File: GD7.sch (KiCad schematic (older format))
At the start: 19 parts, among them IC3 HCPL-316J, IC4 IXDD614PI, P10 CONN_01X03, P11 CONN_01X03

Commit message: uding HCPL-361J modified symbol
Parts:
- IC3: symbol HCPL-316J-RESCUE-gatedrive -> HCPL-316J
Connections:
- wire segments 41 -> 50
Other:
- moved on the sheet: IC4
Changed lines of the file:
@@
 EESchema Schematic File Version 2
-LIBS:gatedrive-rescue
 LIBS:power
 LIBS:device
@@
 LIBS:contrib
 LIBS:valves
-LIBS:GateDrive
+LIBS:74xgxx
+LIBS:ac-dc
+LIBS:actel
+LIBS:Altera
+LIBS:analog_devices
+LIBS:brooktre
+LIBS:cmos_ieee
+LIBS:dc-dc
+LIBS:diode
+LIBS:elec-unifil
+LIBS:ESD_Protection
+LIBS:ftdi
+LIBS:gennum
+LIBS:graphic
+LIBS:hc11
+LIBS:ir
+LIBS:Lattice
+LIBS:logo
+LIBS:maxim
+LIBS:microchip_dspic33dsc
+LIBS:microchip_pic10mcu
+LIBS:microchip_pic12mcu
+LIBS:microchip_pic16mcu
+LIBS:microchip_pic18mcu
+LIBS:microchip_pic32mcu
+LIBS:motor_drivers
+LIBS:msp430
+LIBS:nordicsemi
+LIBS:nxp_armmcu
+LIBS:onsemi
+LIBS:Oscillators
+LIBS:powerint
+LIBS:Power_Management
+LIBS:pspice
+LIBS:references
+LIBS:relays
+LIBS:rfcom
+LIBS:sensors
+LIBS:silabs
+LIBS:stm8
+LIBS:stm32
+LIBS:supertex
+LIBS:switches
+LIBS:transf
+LIBS:ttl_ieee
+LIBS:video
+LIBS:Worldsemi
+LIBS:Xicor
+LIBS:Zilog
 LIBS:gatedrive-cache
 EELAYER 25 0
@@
 L IXDD614PI-RESCUE-gatedrive IC4
 U 1 1 56EFA9D0
-P 7900 5100
-F 0 "IC4" H 7900 4900 60  0000 C CNN
-F 1 "IXDD614PI" H 7950 5450 60  0000 C CNN
-F 2 "gatedrive:DIP-8_W7.62mm_LongPads" H 7900 5200 60  0001 C CNN
-F 3 "" H 7900 5200 60  0000 C CNN
-F 4 "CHINA[already bought]" H 7900 5100 60  0001 C CNN "Supplier"
-	1    7900 5100
-	1    0    0    -1
-$EndComp
-$Comp
-L HCPL-316J-RESCUE-gatedrive IC3
+P 7950 5100
+AR Path="/56EFA9D0" Ref="IC4"  Part="1"
+AR Path="/56EF0567/56EFA9D0" Ref="IC4"  Part="1"
+F 0 "IC4" H 7950 4900 60  0000 C CNN
+F 1 "IXDD614PI" H 8000 5450 60  0000 C CNN
+F 2 "gatedrive:DIP-8_W7.62mm_LongPads" H 7950 5200 60  0001 C CNN
+F 3 "" H 7950 5200 60  0000 C CNN
+F 4 "CHINA[already bought]" H 7950 5100 60  0001 C CNN "Supplier"
+	1    7950 5100
+	1    0    0    -1
+$EndComp
+$Comp
+L HCPL-316J IC3
 U 1 1 56EFA9D1
-P 5550 4750
-F 0 "IC3" H 5550 4150 60  0000 C CNN
-F 1 "HCPL-316J" H 5300 5200 60  0000 C CNN
-F 2 "Housings_SOIC:SOIC-16_7.5x10.3mm_Pitch1.27mm" H 5550 4750 60  0001 C CNN
-F 3 "" H 5550 4750 60  0000 C CNN
-F 4 "CHINA [ already bought]" H 5550 4750 60  0001 C CNN "Supplier"
-	1    5550 4750
+P 5650 4850
+F 0 "IC3" H 5350 4400 60  0000 C CNN
+F 1 "HCPL-316J" H 5400 5350 60  0000 C CNN
+F 2 "Housings_SOIC:SOIC-16_7.5x10.3mm_Pitch1.27mm" H 5650 4850 60  0001 C CNN
+F 3 "" H 5650 4850 60  0000 C CNN
+F 4 "CHINA [ already bought]" H 5650 4850 60  0001 C CNN "Supplier"
+	1    5650 4850
 	1    0    0    -1
 $EndComp
@@
 Text GLabel 6450 4800 2    60   Input ~ 0
 15V7
-Text GLabel 7500 4850 0    60   Input ~ 0
-15V7
-Text GLabel 7500 5150 0    60   Input ~ 0
--5V7
-Text GLabel 8350 5150 2    60   Input ~ 0
+Text GLabel 7550 4850 0    60   Input ~ 0
+15V7
+Text GLabel 7550 5150 0    60   Input ~ 0
+-5V7
+Text GLabel 8300 5150 2    60   Input ~ 0
 -5V7
 Text GLabel 10200 4950 2    60   Input ~ 0
@@
 a cap to ensure soft turn-off, recommended by datasheet of hcpl.
 Wire Wire Line
-	6950 4950 7500 4950
-Wire Wire Line
-	6250 4950 6650 4950
-Wire Wire Line
-	6250 5050 6250 5150
-Wire Wire Line
-	6250 4750 6250 4850
+	6950 4950 7150 4950
+Wire Wire Line
+	7150 4950 7550 4950
+Wire Wire Line
+	5850 4950 6500 4950
+Wire Wire Line
+	6500 4950 6650 4950
+Wire Wire Line
+	5850 5050 6250 5100
+Wire Wire Line
+	6250 5100 5850 5150
+Wire Wire Line
+	5850 4750 6250 4800
+Wire Wire Line
+	6250 4800 5850 4850
 Connection ~ 6550 4100
 Wire Wire Line
-	6550 4650 6250 4650
+	6550 4650 5850 4650
 Wire Wire Line
 	6550 4100 6650 4100
 Wire Wire Line
-	6550 4050 6550 4650
+	6550 4050 6550 4100
+Wire Wire Line
+	6550 4100 6550 4650
 Connection ~ 8450 4950
 Wire Wire Line
@@
 Connection ~ 7150 4950
 Wire Wire Line
-	3625 4650 4850 4650
-Wire Wire Line
-	8350 4950 9050 4950
+	3625 4650 4000 4650
+Wire Wire Line
+	4000 4650 4950 4650
+Wire Wire Line
+	8300 4950 8450 4950
+Wire Wire Line
+	8450 4950 8900 4950
+Wire Wire Line
+	8900 4950 9050 4950
 Wire Wire Line
 	9350 4950 9450 4950
 Wire Wire Line
-	9750 4950 10200 4950
+	9750 4950 9950 4950
+Wire Wire Line
+	9950 4950 10200 4950
 Wire Wire Line
 	9750 5250 9950 5250
@@
 Connection ~ 9950 4950
 Wire Wire Line
-	8350 5050 8450 5050
+	8300 5050 8450 5050
 Wire Wire Line
 	8450 5050 8450 4950
@@
 	4400 4350 4400 4550
 Wire Wire Line
-	4400 4550 4850 4550
+	4400 4550 4950 4550
 Wire Wire Line
 	4000 4350 4000 4650
@@
 	4000 5300 4000 4750
 Wire Wire Line
-	4000 4750 4850 4750
-Wire Wire Line
-	4850 5150 4750 5150
+	4000 4750 4950 4750
+Wire Wire Line
+	4950 5150 4750 5150
 Wire Wire Line
 	4750 5150 4750 5300
 Wire Wire Line
-	4850 4850 4400 4850
+	4950 4850 4400 4850
 Wire Wire Line
 	4400 4850 4400 5300
 Wire Wire Line
-	6250 4450 6300 4450
+	5850 4450 6300 4450
 Wire Wire Line
 	6300 4450 6300 4350
@@
 Wire Wire Line
 	6500 5000 6500 4950
-Text GLabel 8350 4850 2    60   Input ~ 0
+Text GLabel 8300 4850 2    60   Input ~ 0
 15V7
 Text GLabel 7125 5100 3    60   Input ~ 0
 15V7
 Wire Wire Line
-	7125 5050 7500 5050
+	7125 5050 7550 5050
 Text HLabel 900  3800 3    60   Input ~ 0
 T7
-Text HLabel 4850 4450 0    60   Input ~ 0
+Text HLabel 4950 4450 0    60   Input ~ 0
 T7
 Text GLabel 4450 2300 3    60   Input ~ 0
@@
 Text GLabel 4400 4350 1    60   Input ~ 0
 GND1
-Text GLabel 4850 4950 0    60   Input ~ 0
+Text GLabel 4950 4950 0    60   Input ~ 0
 ~FAULT
 Text GLabel 4750 5300 3    60   Input ~ 0

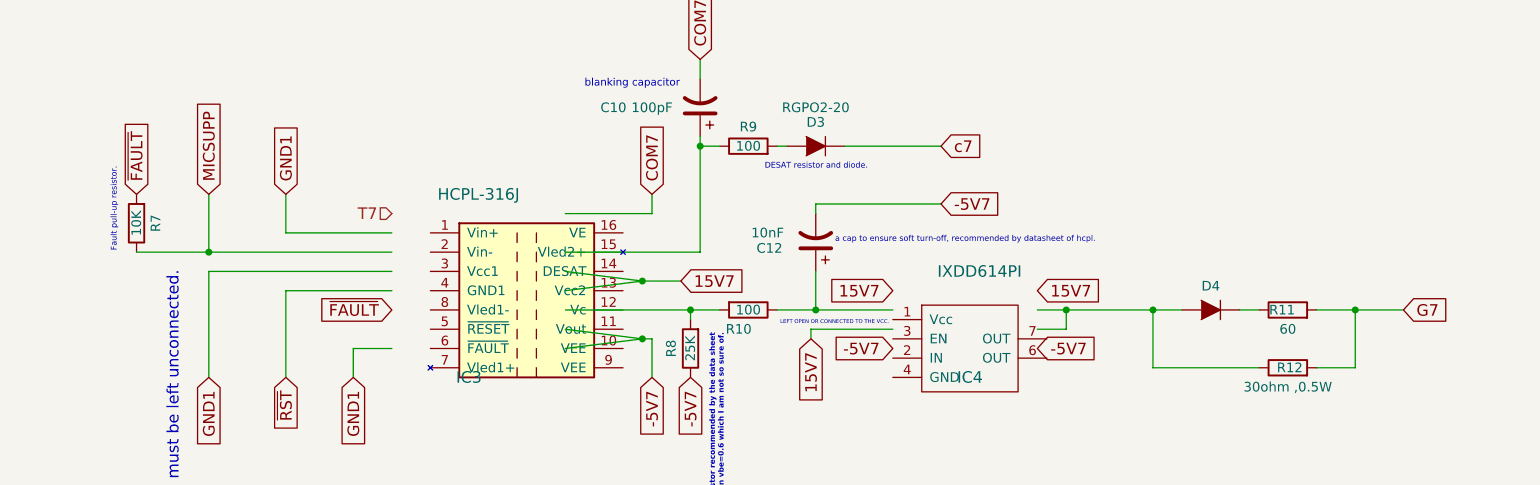
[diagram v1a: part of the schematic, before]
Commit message: cleaning the schematic
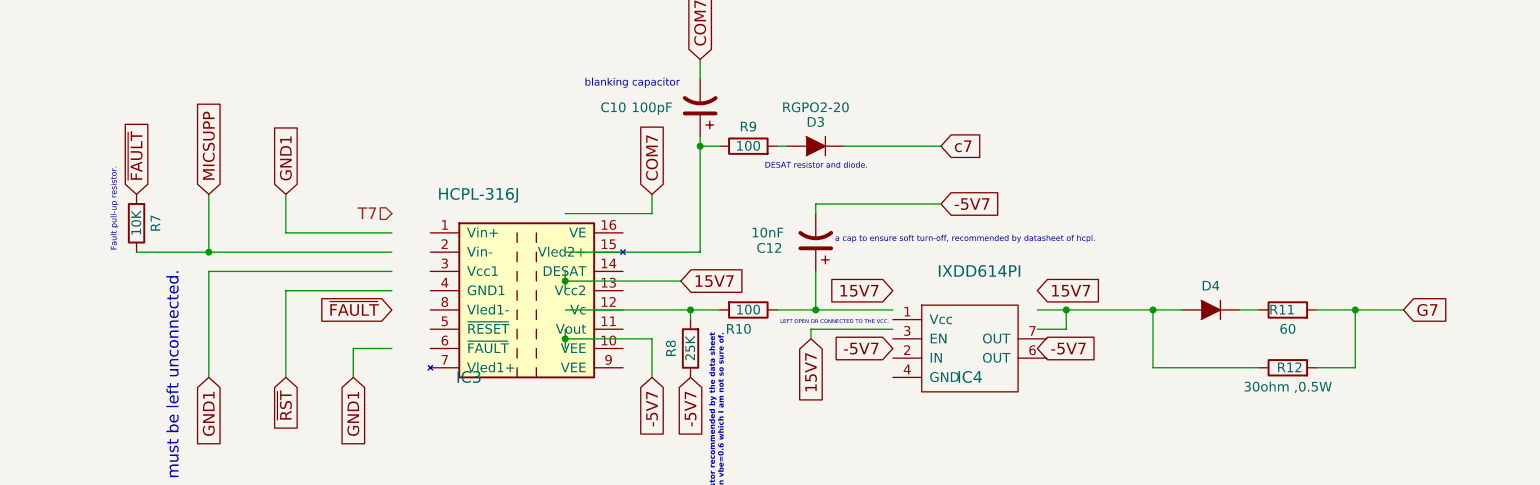
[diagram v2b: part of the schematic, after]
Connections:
- wire segments 50 -> 41
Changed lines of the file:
@@
 a cap to ensure soft turn-off, recommended by datasheet of hcpl.
 Wire Wire Line
-	6950 4950 7150 4950
+	6950 4950 7550 4950
 Wire Wire Line
-	7150 4950 7550 4950
+	5850 4950 6650 4950
 Wire Wire Line
-	5850 4950 6500 4950
+	5850 5050 5850 5150
 Wire Wire Line
-	6500 4950 6650 4950
-Wire Wire Line
-	5850 5050 6250 5100
-Wire Wire Line
-	6250 5100 5850 5150
-Wire Wire Line
-	5850 4750 6250 4800
-Wire Wire Line
-	6250 4800 5850 4850
+	5850 4750 5850 4850
 Connection ~ 6550 4100
 Wire Wire Line
@@
 	6550 4100 6650 4100
 Wire Wire Line
-	6550 4050 6550 4100
-Wire Wire Line
-	6550 4100 6550 4650
+	6550 4050 6550 4650
 Connection ~ 8450 4950
 Wire Wire Line
@@
 Connection ~ 7150 4950
 Wire Wire Line
-	3625 4650 4000 4650
+	3625 4650 4950 4650
 Wire Wire Line
-	4000 4650 4950 4650
-Wire Wire Line
-	8300 4950 8450 4950
-Wire Wire Line
-	8450 4950 8900 4950
-Wire Wire Line
-	8900 4950 9050 4950
+	8300 4950 9050 4950
 Wire Wire Line
 	9350 4950 9450 4950
 Wire Wire Line
-	9750 4950 9950 4950
-Wire Wire Line
-	9950 4950 10200 4950
+	9750 4950 10200 4950
 Wire Wire Line
 	9750 5250 9950 5250
@@
 	6300 5300 6300 5100
 Wire Wire Line
-	6300 5100 6250 5100
-Connection ~ 6250 5100
+	6300 5100 5850 5100
+Connection ~ 5850 5100
 Wire Wire Line
-	6250 4800 6450 4800
-Connection ~ 6250 4800
+	5850 4800 6450 4800
+Connection ~ 5850 4800
 Wire Wire Line
 	8900 5250 9450 5250

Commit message: completion of the layout, initial layout of the protection circuit, reducing number of circuit to 7
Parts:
- C10, C11, C12, C13, C14, C8, C9: footprint Capacitors_ThroughHole:C_Disc_D3_P2.5 -> gatedrive:C_Disc
- D3: footprint Diodes_ThroughHole:Diode_DO-201AD_Horizontal_RM15 -> Diodes_ThroughHole:Diode_DO-41_SOD81_Horizontal_RM10
- R11, R12: footprint Resistors_ThroughHole:Resistor_Horizontal_RM20mm -> gatedrive:Resistor_multi
- R7: footprint Resistors_ThroughHole:Resistor_Vertical_RM5mm -> Resistors_ThroughHole:Resistor_Horizontal_RM10mm
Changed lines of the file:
@@
 EESchema Schematic File Version 2
+LIBS:Symbols_DCDC-ACDC-Converter_RevC_20Jul2012
+LIBS:Symbols_EN60617_13Mar2013
+LIBS:Symbols_EN60617-10_HF-Radio_DRAFT_12Sep2013
+LIBS:Symbols_ICs-Diskrete_RevD10
+LIBS:Symbols_ICs-Opto_RevB_16Sep2013
+LIBS:Symbols_Microcontroller_Philips-NXP_RevA_06Oct2013
+LIBS:SymbolsSimilarEN60617+oldDIN617-RevE8
+LIBS:Symbols_Socket-DIN41612_RevA
+LIBS:Symbols_Transformer-Diskrete_RevA
 LIBS:power
 LIBS:device
@@
 $Descr A4 11693 8268
 encoding utf-8
-Sheet 3 10
+Sheet 3 9
 Title "IGBT GATE DRIVE SCHEMATIC."
 Date "2016-03-02"
@@
 F 0 "D3" H 7150 3976 50  0000 C CNN
 F 1 "RGPO2-20" H 7150 3900 50  0000 C CNN
-F 2 "Diodes_ThroughHole:Diode_DO-201AD_Horizontal_RM15" H 7150 4100 50  0001 C CNN
+F 2 "Diodes_ThroughHole:Diode_DO-41_SOD81_Horizontal_RM10" H 7150 4100 50  0001 C CNN
 F 3 "" H 7150 4100 50  0000 C CNN
 F 4 "El-Amir" H 7150 4100 60  0001 C CNN "Supplier"
@@
 F 0 "R7" V 3525 4500 50  0000 C CNN
 F 1 "10K" V 3625 4500 50  0000 C CNN
-F 2 "Resistors_ThroughHole:Resistor_Vertical_RM5mm" V 3555 4500 50  0001 C CNN
+F 2 "Resistors_ThroughHole:Resistor_Horizontal_RM10mm" V 3555 4500 50  0001 C CNN
 F 3 "" H 3625 4500 50  0000 C CNN
 F 4 "EL AMIR" H 3625 4500 60  0001 C CNN "Supplier"
@@
 F 0 "C8" H 4150 2150 50  0000 C CNN
 F 1 "0.1uF" H 4250 2050 50  0000 C CNN
-F 2 "Capacitors_ThroughHole:C_Disc_D3_P2.5" H 4488 2000 50  0001 C CNN
+F 2 "gatedrive:C_Disc" H 4488 2000 50  0001 C CNN
 F 3 "" H 4450 2150 50  0000 C CNN
 F 4 "EL AMIR" H 4450 2150 60  0001 C CNN "Supplier"
@@
 F 0 "C10" H 7000 3900 50  0000 C CNN
 F 1 "100pF" H 6800 3900 50  0000 C CNN
-F 2 "Capacitors_ThroughHole:C_Disc_D3_P2.5" H 6588 3750 50  0001 C CNN
+F 2 "gatedrive:C_Disc" H 6588 3750 50  0001 C CNN
 F 3 "" H 6550 3900 50  0000 C CNN
 	1    6550 3900
@@
 F 0 "C14" H 8450 2150 50  0000 C CNN
 F 1 "0.1uF" H 8450 2050 50  0000 C CNN
-F 2 "Capacitors_ThroughHole:C_Disc_D3_P2.5" H 8888 2000 50  0001 C CNN
+F 2 "gatedrive:C_Disc" H 8888 2000 50  0001 C CNN
 F 3 "" H 8850 2150 50  0000 C CNN
 	1    8850 2150
@@
 F 0 "C13" H 7400 2150 50  0000 C CNN
 F 1 "0.1uF" H 7400 2050 50  0000 C CNN
-F 2 "Capacitors_ThroughHole:C_Disc_D3_P2.5" H 7788 2000 50  0001 C CNN
+F 2 "gatedrive:C_Disc" H 7788 2000 50  0001 C CNN
 F 3 "" H 7750 2150 50  0000 C CNN
 	1    7750 2150
@@
 F 0 "C9" H 5150 2150 50  0000 C CNN
 F 1 "0.1uF" H 5150 2050 50  0000 C CNN
-F 2 "Capacitors_ThroughHole:C_Disc_D3_P2.5" H 5538 2000 50  0001 C CNN
+F 2 "gatedrive:C_Disc" H 5538 2000 50  0001 C CNN
 F 3 "" H 5500 2150 50  0000 C CNN
 	1    5500 2150
@@
 F 0 "C11" H 6300 2150 50  0000 R CNN
 F 1 "330pF" H 6400 2050 50  0000 R CNN
-F 2 "Capacitors_ThroughHole:C_Disc_D3_P2.5" H 6638 2000 50  0001 C CNN
+F 2 "gatedrive:C_Disc" H 6638 2000 50  0001 C CNN
 F 3 "" H 6600 2150 50  0000 C CNN
 	1    6600 2150
@@
 LEFT OPEN OR CONNECTED TO THE VCC.
 $Comp
-L PWR_FLAG #FLG08
+L PWR_FLAG #FLG01
 U 1 1 56EFA9DE
 P 1300 3800
-F 0 "#FLG08" H 1300 3895 50  0001 C CNN
+F 0 "#FLG01" H 1300 3895 50  0001 C CNN
 F 1 "PWR_FLAG" H 1300 4024 50  0000 C CNN
 F 2 "" H 1300 3800 50  0000 C CNN
@@
 $EndComp
 $Comp
-L PWR_FLAG #FLG09
+L PWR_FLAG #FLG02
 U 1 1 56EFA9DF
 P 1750 3800
-F 0 "#FLG09" H 1750 3895 50  0001 C CNN
+F 0 "#FLG02" H 1750 3895 50  0001 C CNN
 F 1 "PWR_FLAG" H 1750 4024 50  0000 C CNN
 F 2 "" H 1750 3800 50  0000 C CNN
@@
 $EndComp
 $Comp
-L PWR_FLAG #FLG010
+L PWR_FLAG #FLG03
 U 1 1 56EFA9E0
 P 1750 2650
-F 0 "#FLG010" H 1750 2745 50  0001 C CNN
+F 0 "#FLG03" H 1750 2745 50  0001 C CNN
 F 1 "PWR_FLAG" H 1750 2874 50  0000 C CNN
 F 2 "" H 1750 2650 50  0000 C CNN
@@
 $EndComp
 $Comp
-L PWR_FLAG #FLG011
+L PWR_FLAG #FLG04
 U 1 1 56EFA9E1
 P 900 2650
-F 0 "#FLG011" H 900 2745 50  0001 C CNN
+F 0 "#FLG04" H 900 2745 50  0001 C CNN
 F 1 "PWR_FLAG" H 900 2874 50  0000 C CNN
 F 2 "" H 900 2650 50  0000 C CNN
@@
 $EndComp
 $Comp
-L PWR_FLAG #FLG012
+L PWR_FLAG #FLG05
 U 1 1 56EFA9E2
 P 1300 2650
-F 0 "#FLG012" H 1300 2745 50  0001 C CNN
+F 0 "#FLG05" H 1300 2745 50  0001 C CNN
 F 1 "PWR_FLAG" H 1300 2874 50  0000 C CNN
 F 2 "" H 1300 2650 50  0000 C CNN
@@
 $EndComp
 $Comp
-L PWR_FLAG #FLG013
+L PWR_FLAG #FLG06
 U 1 1 56EFA9E3
 P 900 3800
-F 0 "#FLG013" H 900 3895 50  0001 C CNN
+F 0 "#FLG06" H 900 3895 50  0001 C CNN
 F 1 "PWR_FLAG" H 900 4024 50  0000 C CNN
 F 2 "" H 900 3800 50  0000 C CNN
@@
 F 0 "C12" H 7390 4630 50  0000 C CNN
 F 1 "10nF" H 7400 4550 50  0000 C CNN
-F 2 "Capacitors_ThroughHole:C_Disc_D3_P2.5" H 7188 4450 50  0001 C CNN
+F 2 "gatedrive:C_Disc" H 7188 4450 50  0001 C CNN
 F 3 "" H 7150 4600 50  0000 C CNN
 	1    7150 4600
@@
 F 0 "R11" V 9600 4980 50  0000 C CNN
 F 1 "60" V 9500 4950 50  0000 C CNN
-F 2 "Resistors_ThroughHole:Resistor_Horizontal_RM20mm" V 9530 4950 50  0001 C CNN
+F 2 "gatedrive:Resistor_multi" V 9530 4950 50  0001 C CNN
 F 3 "" H 9600 4950 50  0000 C CNN
 F 4 "Al amir" H 9600 4950 60  0001 C CNN "Supplier"
@@
 F 0 "R12" V 9600 5240 50  0000 C CNN
 F 1 "30ohm ,0.5W" V 9500 5250 50  0000 C CNN
-F 2 "Resistors_ThroughHole:Resistor_Horizontal_RM20mm" V 9530 5250 50  0001 C CNN
+F 2 "gatedrive:Resistor_multi" V 9530 5250 50  0001 C CNN
 F 3 "" H 9600 5250 50  0000 C CNN
 F 4 "Supplier_name" H 9600 5250 60  0001 C CNN "Supplier"
@@
 	6950 4100 7000 4100
 $Comp
-L PWR_FLAG #FLG014
+L PWR_FLAG #FLG07
 U 1 1 56EFA9EA
 P 1475 3050
-F 0 "#FLG014" H 1475 3145 50  0001 C CNN
+F 0 "#FLG07" H 1475 3145 50  0001 C CNN
 F 1 "PWR_FLAG" V 1625 3050 50  0000 C CNN
 F 2 "" H 1475 3050 50  0000 C CNN
@@
 Text GLabel 1150 4900 2    60   Input ~ 0
 COM7
-Text GLabel 1250 5300 2    60   Input ~ 0
+Text GLabel 1250 5500 2    60   Input ~ 0
 G7
 Text GLabel 1250 5400 2    60   Input ~ 0
 c7
-Text GLabel 1250 5500 2    60   Input ~ 0
+Text GLabel 1250 5300 2    60   Input ~ 0
 COM7
 $EndSCHEMATC

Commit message: yet another enhancements .
the protection section still is incomplete.
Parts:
- IC4: symbol IXDD614PI-RESCUE-gatedrive -> IXDD614PI
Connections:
- wire segments 41 -> 50
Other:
- moved on the sheet: IC3
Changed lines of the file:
@@
 $Descr A4 11693 8268
 encoding utf-8
-Sheet 3 9
+Sheet 2 9
 Title "IGBT GATE DRIVE SCHEMATIC."
 Date "2016-03-02"
@@
 $EndDescr
 $Comp
-L IXDD614PI-RESCUE-gatedrive IC4
+L IXDD614PI IC4
 U 1 1 56EFA9D0
-P 7950 5100
+P 7950 4950
 AR Path="/56EFA9D0" Ref="IC4"  Part="1"
 AR Path="/56EF0567/56EFA9D0" Ref="IC4"  Part="1"
-F 0 "IC4" H 7950 4900 60  0000 C CNN
-F 1 "IXDD614PI" H 8000 5450 60  0000 C CNN
-F 2 "gatedrive:DIP-8_W7.62mm_LongPads" H 7950 5200 60  0001 C CNN
-F 3 "" H 7950 5200 60  0000 C CNN
-F 4 "CHINA[already bought]" H 7950 5100 60  0001 C CNN "Supplier"
-	1    7950 5100
+F 0 "IC4" H 7950 4750 60  0000 C CNN
+F 1 "IXDD614PI" H 8000 5300 60  0000 C CNN
+F 2 "gatedrive:DIP-8_W7.62mm_LongPads" H 7950 5050 60  0001 C CNN
+F 3 "" H 7950 5050 60  0000 C CNN
+F 4 "CHINA[already bought]" H 7950 4950 60  0001 C CNN "Supplier"
+	1    7950 4950
 	1    0    0    -1
 $EndComp
@@
 L HCPL-316J IC3
 U 1 1 56EFA9D1
-P 5650 4850
-F 0 "IC3" H 5350 4400 60  0000 C CNN
-F 1 "HCPL-316J" H 5400 5350 60  0000 C CNN
-F 2 "Housings_SOIC:SOIC-16_7.5x10.3mm_Pitch1.27mm" H 5650 4850 60  0001 C CNN
-F 3 "" H 5650 4850 60  0000 C CNN
-F 4 "CHINA [ already bought]" H 5650 4850 60  0001 C CNN "Supplier"
-	1    5650 4850
+P 5350 4750
+AR Path="/56EFA9D1" Ref="IC3"  Part="1"
+AR Path="/56EF0567/56EFA9D1" Ref="IC3"  Part="1"
+F 0 "IC3" H 5050 4300 60  0000 C CNN
+F 1 "HCPL-316J" H 5100 5250 60  0000 C CNN
+F 2 "Housings_SOIC:SOIC-16_7.5x10.3mm_Pitch1.27mm" H 5350 4750 60  0001 C CNN
+F 3 "" H 5350 4750 60  0000 C CNN
+F 4 "CHINA [ already bought]" H 5350 4750 60  0001 C CNN "Supplier"
+	1    5350 4750
 	1    0    0    -1
 $EndComp
@@
 Text GLabel 7550 5150 0    60   Input ~ 0
 -5V7
-Text GLabel 8300 5150 2    60   Input ~ 0
+Text GLabel 8350 5150 2    60   Input ~ 0
 -5V7
 Text GLabel 10200 4950 2    60   Input ~ 0
@@
 a cap to ensure soft turn-off, recommended by datasheet of hcpl.
 Wire Wire Line
-	6950 4950 7550 4950
-Wire Wire Line
-	5850 4950 6650 4950
-Wire Wire Line
-	5850 5050 5850 5150
-Wire Wire Line
-	5850 4750 5850 4850
+	6950 4950 7150 4950
+Wire Wire Line
+	7150 4950 7550 4950
+Wire Wire Line
+	5850 4950 6500 4950
+Wire Wire Line
+	6500 4950 6650 4950
+Wire Wire Line
+	5850 5050 5850 5100
+Wire Wire Line
+	5850 5100 5850 5150
+Wire Wire Line
+	5850 4750 5850 4800
+Wire Wire Line
+	5850 4800 5850 4850
 Connection ~ 6550 4100
 Wire Wire Line
@@
 	6550 4100 6650 4100
 Wire Wire Line
-	6550 4050 6550 4650
+	6550 4050 6550 4100
+Wire Wire Line
+	6550 4100 6550 4650
 Connection ~ 8450 4950
 Wire Wire Line
@@
 Connection ~ 7150 4950
 Wire Wire Line
-	3625 4650 4950 4650
-Wire Wire Line
-	8300 4950 9050 4950
+	3625 4650 4000 4650
+Wire Wire Line
+	4000 4650 4850 4650
+Wire Wire Line
+	8350 4950 8450 4950
+Wire Wire Line
+	8450 4950 8900 4950
+Wire Wire Line
+	8900 4950 9050 4950
 Wire Wire Line
 	9350 4950 9450 4950
 Wire Wire Line
-	9750 4950 10200 4950
+	9750 4950 9950 4950
+Wire Wire Line
+	9950 4950 10200 4950
 Wire Wire Line
 	9750 5250 9950 5250
@@
 Connection ~ 9950 4950
 Wire Wire Line
-	8300 5050 8450 5050
+	8350 5050 8450 5050
 Wire Wire Line
 	8450 5050 8450 4950
@@
 	4400 4350 4400 4550
 Wire Wire Line
-	4400 4550 4950 4550
+	4400 4550 4850 4550
 Wire Wire Line
 	4000 4350 4000 4650
@@
 	4000 5300 4000 4750
 Wire Wire Line
-	4000 4750 4950 4750
-Wire Wire Line
-	4950 5150 4750 5150
+	4000 4750 4850 4750
+Wire Wire Line
+	4850 5150 4750 5150
 Wire Wire Line
 	4750 5150 4750 5300
 Wire Wire Line
-	4950 4850 4400 4850
+	4850 4850 4400 4850
 Wire Wire Line
 	4400 4850 4400 5300
@@
 Wire Wire Line
 	6500 5000 6500 4950
-Text GLabel 8300 4850 2    60   Input ~ 0
+Text GLabel 8350 4850 2    60   Input ~ 0
 15V7
 Text GLabel 7125 5100 3    60   Input ~ 0
@@
 Text HLabel 900  3800 3    60   Input ~ 0
 T7
-Text HLabel 4950 4450 0    60   Input ~ 0
+Text HLabel 4850 4450 0    60   Input ~ 0
 T7
 Text GLabel 4450 2300 3    60   Input ~ 0
@@
 Text GLabel 4400 4350 1    60   Input ~ 0
 GND1
-Text GLabel 4950 4950 0    60   Input ~ 0
+Text GLabel 4850 4950 0    60   Input ~ 0
 ~FAULT
 Text GLabel 4750 5300 3    60   Input ~ 0
